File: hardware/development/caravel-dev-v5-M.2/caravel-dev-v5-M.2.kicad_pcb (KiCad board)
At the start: 2 copper layers, 76.2 x 73.8 mm, 64 parts, among them J1 USB_B_Micro - 10118193-0001LF, J10 Conn_01x27_Female, J11 Conn_01x20_Female, J2 Conn_01x02_Female, J3 Conn_01x02_Male, J4 Conn_01x03_Female, J5 Conn_01x02_Male, J6 Conn_01x02_Male, J7 Conn_01x06_Female, J8 Conn_01x02_Male, J9 Conn_01x02_Male, SW1 SW_Push - SKQGADE010, T1 Logo, T2 Logo, U1 FT232H, U2 SN74LVC1G125DCKR, U3 SN74LVC1G125DCKR, U4 MCP1319MT-29LE-OT, U5 TAR5SxxU_SOT353F, U6 TAR5SxxU_SOT353F, U7 W25Q32FVSS, U8 caravel-M.2-card, X1 DSC6001_10MHZ, Y1 CSTNE12M0GH5L000R0

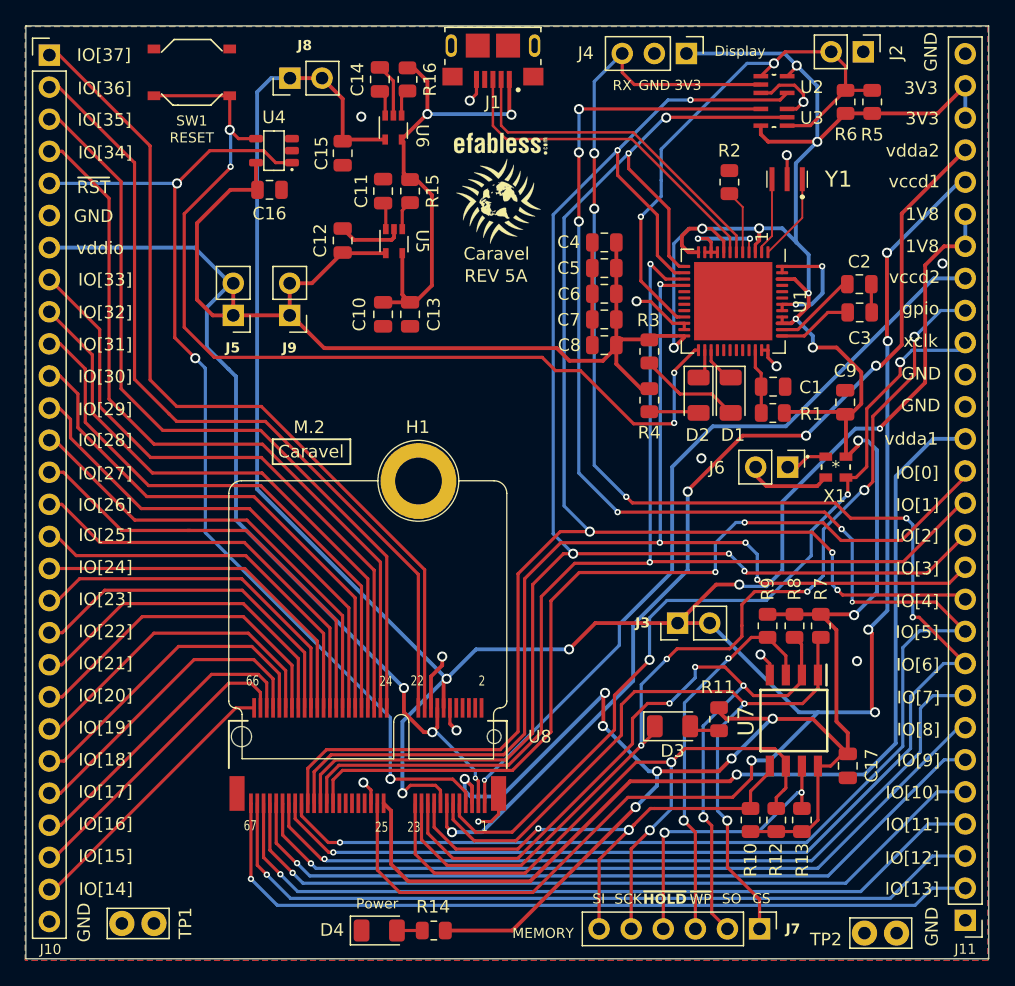
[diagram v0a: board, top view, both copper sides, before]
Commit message: ~ update caravel v5 REV5B
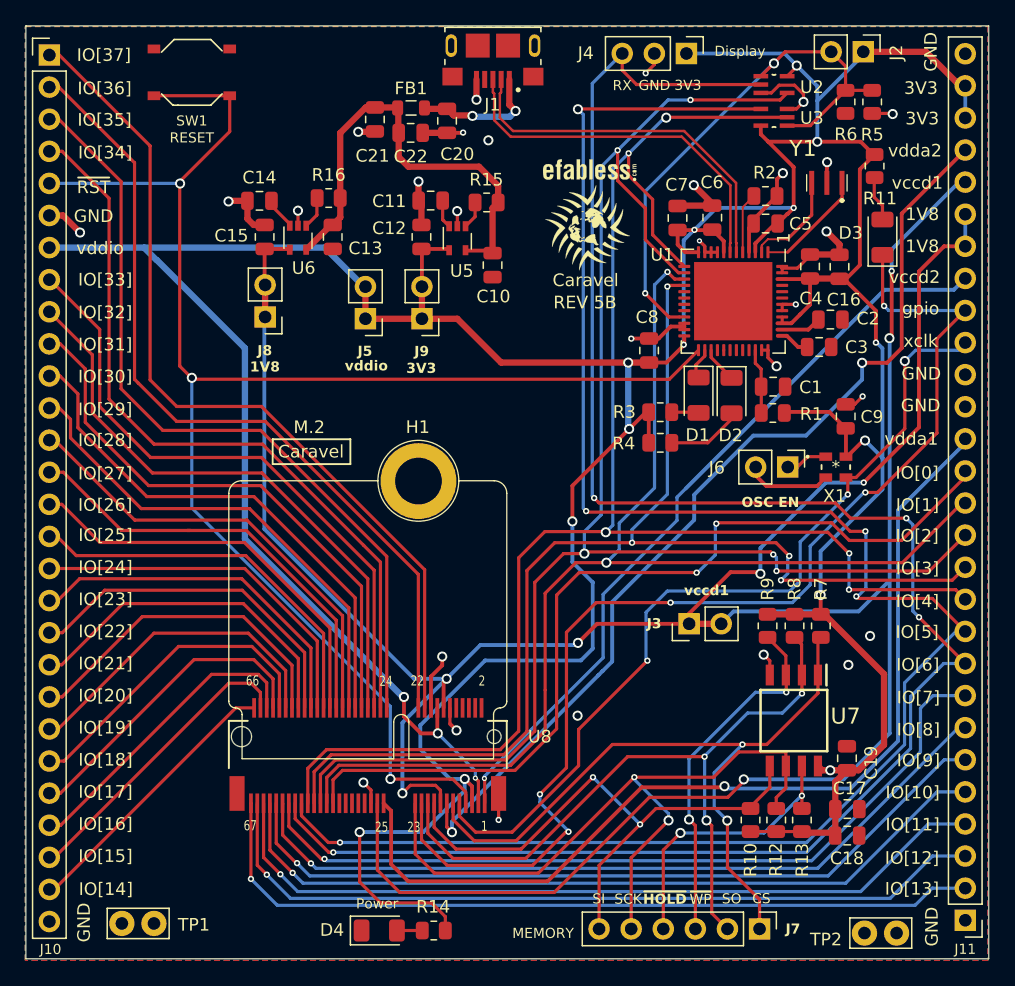
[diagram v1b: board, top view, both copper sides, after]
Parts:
- removed the D1 at (150.8, 146.9)
- removed the R3 at (144.4, 143.4)
- removed U4: MCP1319MT-29LE-OT, Caravel_Board:PoR_5_SOT23
- added C18: 0.1uF, Capacitor_SMD:C_0805_2012Metric, F.Cu at (160.0, 181.8)
- added C19: 1uF, Capacitor_SMD:C_0805_2012Metric, F.Cu at (160.0, 175.6)
- added C20: 0.01uF, Capacitor_SMD:C_0805_2012Metric, F.Cu at (128.4, 125.2)
- added C21: 0.1uF, Capacitor_SMD:C_0805_2012Metric, F.Cu at (122.7, 125.1)
- added C22: 10uF, Capacitor_SMD:C_0805_2012Metric, F.Cu at (125.5, 126.1)
- added D2: RED, LED_SMD:LED_1206_3216Metric, F.Cu at (150.9, 146.9)
- added FB1: 600R/0.5A, Inductor_SMD:L_0805_2012Metric, F.Cu at (125.5, 124.2)
- added R4: 150, Resistor_SMD:R_0805_2012Metric, F.Cu at (145.2, 150.7)
- C1: value 0.01uf - CC0805JRX7R9BB103 -> 0.01uF
- C10, C13: value 1uf - CC0805KKX5R8BB105 -> 1uF
- C11, C14: value 0.01uf - CC0805KRX7R9BB103 -> 0.01uF
- C12, C15: value 10uf - CC0805KKX5R8BB106 -> 10uF
- C16: value 0.1uf - CC0805KRX7R9BB104 -> 10uF
- C17: value 0.1uf - CC0805KRX7R9BB104 -> 0.01uF
- C2, C3, C4, C5, C6, C7, C8, C9: value 0.1uf - CC0805KRX7R9BB104 -> 0.1uF
- D1: renamed from D2; value LED - 17-215SURC/S530-A2/TR8 -> RED
- D3, D4: value LED - 17-215SURC/S530-A2/TR8 -> RED
- J1: value USB_B_Micro - 10118193-0001LF -> USB_B_Micro
- J10: value Conn_01x27_Female -> Conn_01x28_Pin
- J11: value Conn_01x20_Female -> Conn_01x28_Pin
- J2: value Conn_01x02_Female -> Conn_01x02_Pin
- J3, J5, J6, J8, J9: value Conn_01x02_Male -> Conn_01x02_Pin
- J4: value Conn_01x03_Female -> Conn_01x03_Pin
- J7: value Conn_01x06_Female -> Conn_01x06_Pin
- R1, R10, R12, R13, R7, R8, R9: value 10k - RC0805FR-0710KL -> 10K
- R11, R14: value 82 - 0805W8F820JT5E -> 1K
- R15, R16: value 10k -> 10K
- R2: value 12K 1% - 0805W8F1202T5E -> 12K 1%
- R3: renamed from R4; value 150 - 0805W8J0151T5E -> 150
- R5, R6: value 10k -> 1K
- U5, U6: value TAR5SxxU_SOT353F -> TAR5SxxU
- U8: value caravel-M.2-card -> M.2-CONNECTOR-E
- Y1: value CSTNE12M0GH5L000R0 -> 12MHz
- moved C16 45.5 mm to (159.4, 136.7), turned to 90 degrees
- moved R11 45.5 mm to (162.2, 128.8)
- moved D3 42.1 mm to (162.8, 134.4), turned to 90 degrees
- moved J8 19.0 mm to (114.0, 140.7), turned to 180 degrees
- moved C4 16.4 mm to (157.1, 136.7), turned to -90 degrees
- moved C14 13.5 mm to (113.5, 131.5), turned to 180 degrees
- moved C5 13.2 mm to (153.6, 133.3)
- moved U6 11.5 mm to (116.6, 134.4)
- moved R16 11.3 mm to (119.0, 131.3), turned to 0 degrees
- moved J5 10.5 mm to (121.9, 140.9)
- moved J9 10.5 mm to (126.4, 140.9)
- moved C6 10.5 mm to (149.3, 132.8), turned to -90 degrees
- moved C7 9.90 mm to (146.6, 132.9), turned to -90 degrees
- moved C10 9.50 mm to (132.0, 136.6)
- moved C15 9.06 mm to (113.9, 134.4), turned to -90 degrees
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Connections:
- net Caravel_CSB renamed /Caravel_CSB
- net Caravel_D0 renamed /Caravel_D0
- net Caravel_D1 renamed /Caravel_D1
- net Caravel_SCK renamed /Caravel_SCK
- net FTDI_D+ renamed /FTDI_D+
- net FTDI_D- renamed /FTDI_D-
- net Net-(D2-K) renamed /ACBUS2
- net Net-(J6-Pin_1) renamed /OSC_EN
- net Net-(U1-VCCA) renamed /VCCA
- net Net-(U1-VCCCORE) renamed /VCCCORE
- net Net-(U1-~{RESET}) renamed /~{FTDI_RST}
- net Net-(U5-Noise) renamed /Noise_3V3
- net Net-(U6-Noise) renamed /Noise_1V8
- net UART_EN renamed /ACBUS0
- net USB_CS1 renamed /USB_CS1
- net USB_SCK_TXD renamed /USB_SCK_TXD
- net USB_SI renamed /USB_SI
- net USB_SO_RXD renamed /USB_SO_RXD
- net gpio renamed /gpio
- net mprj_io[0] renamed /mprj_io[0]
- net mprj_io[10] renamed /mprj_io[10]
- net mprj_io[11] renamed /mprj_io[11]
- net mprj_io[12] renamed /mprj_io[12]
- net mprj_io[13] renamed /mprj_io[13]
- net mprj_io[14] renamed /mprj_io[14]
- net mprj_io[15] renamed /mprj_io[15]
- net mprj_io[16] renamed /mprj_io[16]
- net mprj_io[17] renamed /mprj_io[17]
- net mprj_io[18] renamed /mprj_io[18]
- net mprj_io[19] renamed /mprj_io[19]
- net mprj_io[20] renamed /mprj_io[20]
- net mprj_io[21] renamed /mprj_io[21]
- net mprj_io[22] renamed /mprj_io[22]
- net mprj_io[23] renamed /mprj_io[23]
- net mprj_io[24] renamed /mprj_io[24]
- net mprj_io[25] renamed /mprj_io[25]
- net mprj_io[26] renamed /mprj_io[26]
- net mprj_io[27] renamed /mprj_io[27]
- net mprj_io[28] renamed /mprj_io[28]
- net mprj_io[29] renamed /mprj_io[29]
- net mprj_io[30] renamed /mprj_io[30]
- net mprj_io[31] renamed /mprj_io[31]
- net mprj_io[32] renamed /mprj_io[32]
- net mprj_io[33] renamed /mprj_io[33]
- net mprj_io[34] renamed /mprj_io[34]
- net mprj_io[35] renamed /mprj_io[35]
- net mprj_io[36] renamed /mprj_io[36]
- net mprj_io[37] renamed /mprj_io[37]
- net mprj_io[5]_ser_rx renamed /mprj_io[5]_ser_rx
- net mprj_io[6]_ser_tx renamed /mprj_io[6]_ser_tx
- net mprj_io[7] renamed /mprj_io[7]
- net mprj_io[8] renamed /mprj_io[8]
- net mprj_io[9] renamed /mprj_io[9]
- net vccd renamed +1V8
- net vccd2 renamed /vccd2
- net vdda1 renamed /vdda1
- net vdda2 renamed /vdda2
- net xclk renamed /xclk
- net ~{MEM_HOLD} renamed /~{MEM_HOLD}
- net ~{MEM_WP} renamed /~{MEM_WP}
- C12 pad 2: vdda -> +3V3
- C16 pad 1: GND -> +3V3
- C16 pad 2: vdda -> GND
- C17 pad 1: vdda -> GND
- C17 pad 2: GND -> +3V3
- C4 pad 2: vdda -> +3V3
- C5 pad 2: vdda -> +3V3
- C6 pad 2: vdda -> +3V3
- C7 pad 2: vdda -> +3V3
- C8 pad 2: vdda -> +3V3
- C9 pad 2: vdda -> +3V3
- J1 pad 1: +5V -> VBUS
- J10 pad 5: ~{RST} -> /ACBUS1
- J10 pad 7: vdda -> +3V3
- J11 pad 26: vdda -> +3V3
- J11 pad 27: vdda -> +3V3
- J2 pad 1: GND -> +3V3
- J4 pad 1: vdda -> +3V3
- J5 pad 1: vdda -> +3V3
- J5 pad 2: vdda -> +3V3
- J9 pad 1: vdda -> +3V3
- J9 pad 2: vdda -> +3V3
- R1 pad 2: vdda -> +3V3
- R10 pad 2: vdda -> +3V3
- R11 pad 1: vdda -> +3V3
- R12 pad 2: vdda -> +3V3
- R13 pad 2: vdda -> +3V3
- R14 pad 1: vdda -> +3V3
- R3 pad 2: vdda -> +3V3
- R5 pad 1: vdda -> GND
- R6 pad 1: vdda -> GND
- R7 pad 2: vdda -> +3V3
- R8 pad 2: vdda -> +3V3
- R9 pad 2: vdda -> +3V3
- SW1 pad 1: ~{MR} -> /ACBUS1
- U1 pad 12: vdda -> +3V3
- U1 pad 17: unconnected-(U1-ADBUS4-Pad17) -> /ADBUS4
- U1 pad 18: unconnected-(U1-ADBUS5-Pad18) -> /ADBUS5
- U1 pad 19: unconnected-(U1-ADBUS6-Pad19) -> /ADBUS6
- U1 pad 20: unconnected-(U1-ADBUS7-Pad20) -> /ADBUS7
- U1 pad 24: vdda -> +3V3
- U1 pad 25: ~{MR} -> /ACBUS1
- U1 pad 27: Net-(D1-K) -> /ACBUS3
- U1 pad 28: unconnected-(U1-ACBUS4-Pad28) -> /ACBUS4
- U1 pad 29: unconnected-(U1-ACBUS5-Pad29) -> /ACBUS5
- U1 pad 3: vdda -> +3V3
- U1 pad 30: unconnected-(U1-ACBUS6-Pad30) -> /ACBUS6
- U1 pad 31: unconnected-(U1-ACBUS7-Pad31) -> /ACBUS7
- U1 pad 39: vdda -> +3V3
- U1 pad 40: vdda -> +3V3
- U1 pad 46: vdda -> +3V3
- U1 pad 8: vdda -> +3V3
- U2 pad 5: vdda -> +3V3
- U3 pad 5: vdda -> +3V3
- U5 pad 4: vdda -> +3V3
- U7 pad 8: vdda -> +3V3
- U8 pad 16: vdda -> +3V3
- U8 pad 3: vdda -> +3V3
- U8 pad 5: vdda -> +3V3
- U8 pad 7: ~{RST} -> /ACBUS1
- X1 pad 4: vdda -> +3V3
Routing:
- net +3V3: track 0.00 -> 382.4 mm, vias 0 -> 17
- net vdda: track 379.7 -> 0.00 mm, vias 20 -> 0
- net /ACBUS1: track 0.00 -> 127.2 mm, vias 0 -> 3
- net ~{RST}: track 82.2 -> 0.00 mm, vias 3 -> 0
- net ~{MR}: track 76.8 -> 0.00 mm, vias 4 -> 0
- net +1V8: track 263.7 -> 243.2 mm, vias 10 -> 8
- net /gpio: track 78.2 -> 92.9 mm
- net VBUS: track 0.00 -> 10.3 mm, vias 0 -> 2
- net /Caravel_D1: track 67.3 -> 57.3 mm, vias 4 -> 3
- net Net-(D1-A) (its old number): track 8.25 -> 0.00 mm
- net GND: track 75.9 -> 82.9 mm, vias 18 -> 29
- net Net-(D2-A): track 0.00 -> 5.97 mm
- net /Caravel_CSB: track 62.3 -> 57.2 mm
- net /VCCCORE: track 7.03 -> 3.58 mm
- net /VCCA: track 6.11 -> 2.74 mm
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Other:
- board text added: "OSC EN"
- board text added: "REV 5B"
- board text removed: "REV 5A"
